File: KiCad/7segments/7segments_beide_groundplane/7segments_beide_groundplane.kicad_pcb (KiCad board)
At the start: 2 copper layers, 72.4 x 55.9 mm, 25 parts, among them J1 Conn_01x04_Female, J2 12V DC, J3 R pinnen RGB strips, SW1 ENABLE, SW2 BOOT, T1 BC848, T2 BC848, T3 BC848, T4 BC848, T5 BC848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

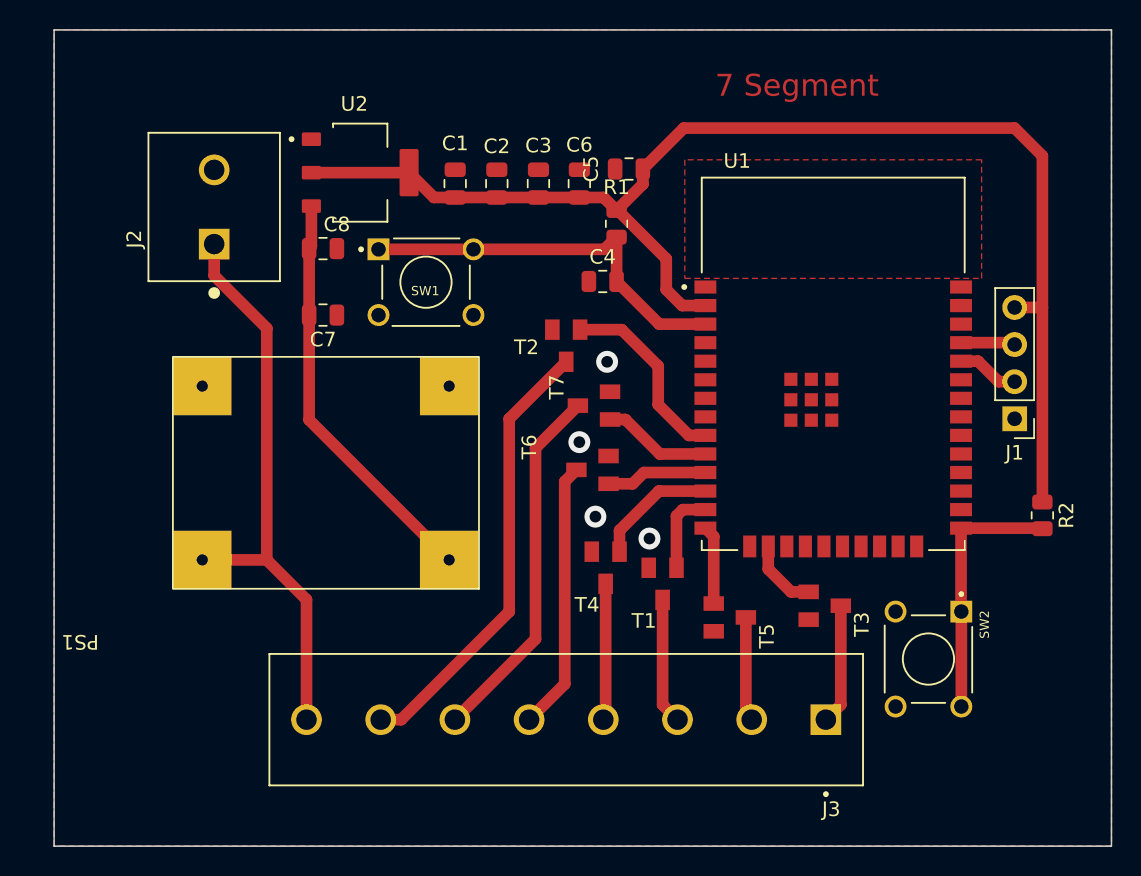
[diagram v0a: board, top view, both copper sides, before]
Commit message: aanpassingen aan kicad ontwerpen van 7segment en buffer
toevoeging van groundplanes
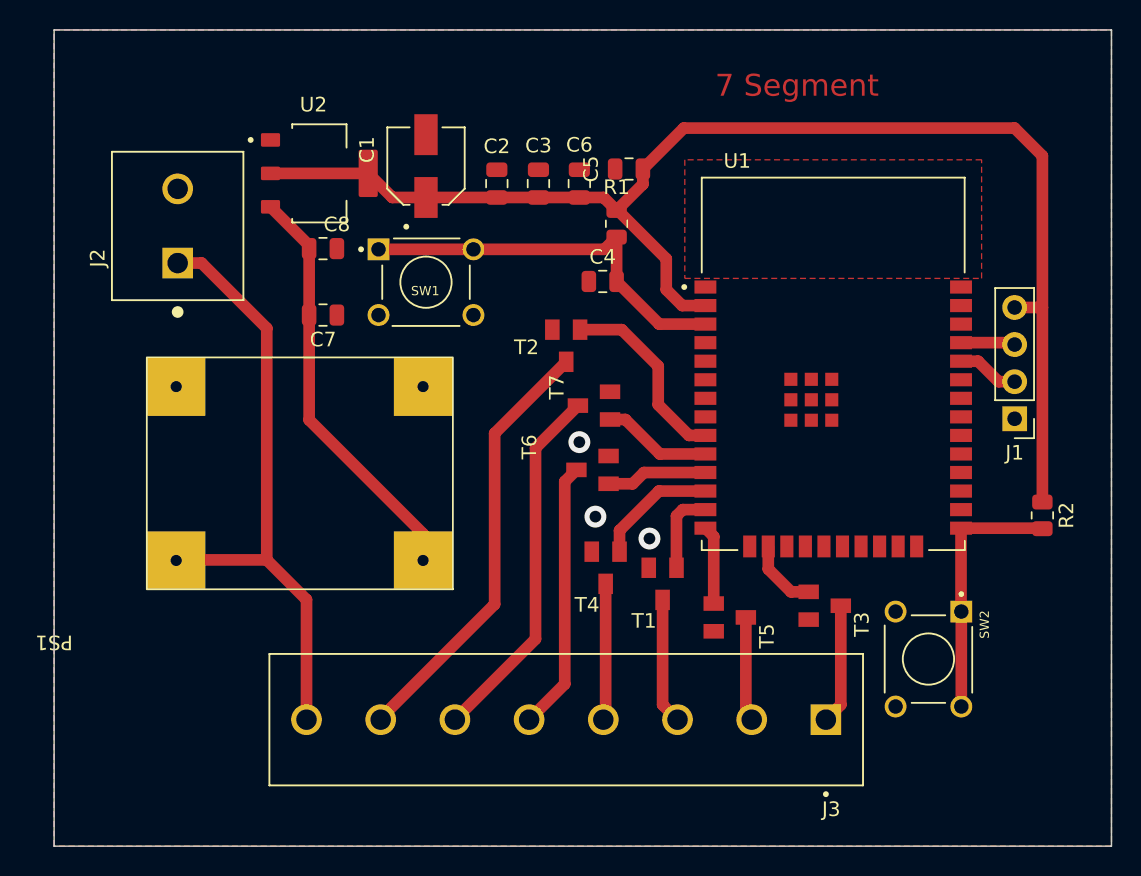
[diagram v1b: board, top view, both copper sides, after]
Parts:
- C1: footprint Capacitor_SMD:C_0805_2012Metric -> libraries:CAP_EEE0JA101WR
- moved J2 2.82 mm to (112.6, 82.0)
- moved U2 2.80 mm to (122.3, 78.4)
- moved C1 2.33 mm to (129.6, 77.9)
- moved PS1 1.79 mm to (120.9, 99.0)
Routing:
- net +3V3: track 90.5 -> 93.2 mm
- net 12V: track 39.6 -> 42.1 mm
- net Net-(J3-Pad7): track 30.6 -> 29.8 mm
- net GND: vias 4 -> 3

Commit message: aanpassingen 11/04 kicad
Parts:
- moved C1 0.58 mm to (130.2, 77.9)
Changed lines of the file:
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@@
   )
   (footprint "libraries:CAP_EEE0JA101WR" (layer "F.Cu")
-    (at 129.6 77.9 90)
+    (at 130.175 77.851 90)
     (property "Sheetfile" "7segments_beide_groundplane.kicad_sch")
     (property "Sheetname" "")
